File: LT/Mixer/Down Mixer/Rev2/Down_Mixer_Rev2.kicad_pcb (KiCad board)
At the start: 2 copper layers, 70.6 x 45.2 mm, 18 parts, among them J1 Conn_Coaxial, J2 Conn_Coaxial, J3 Conn_Coaxial, J4 Conn_01x02_Male, U1 SA602

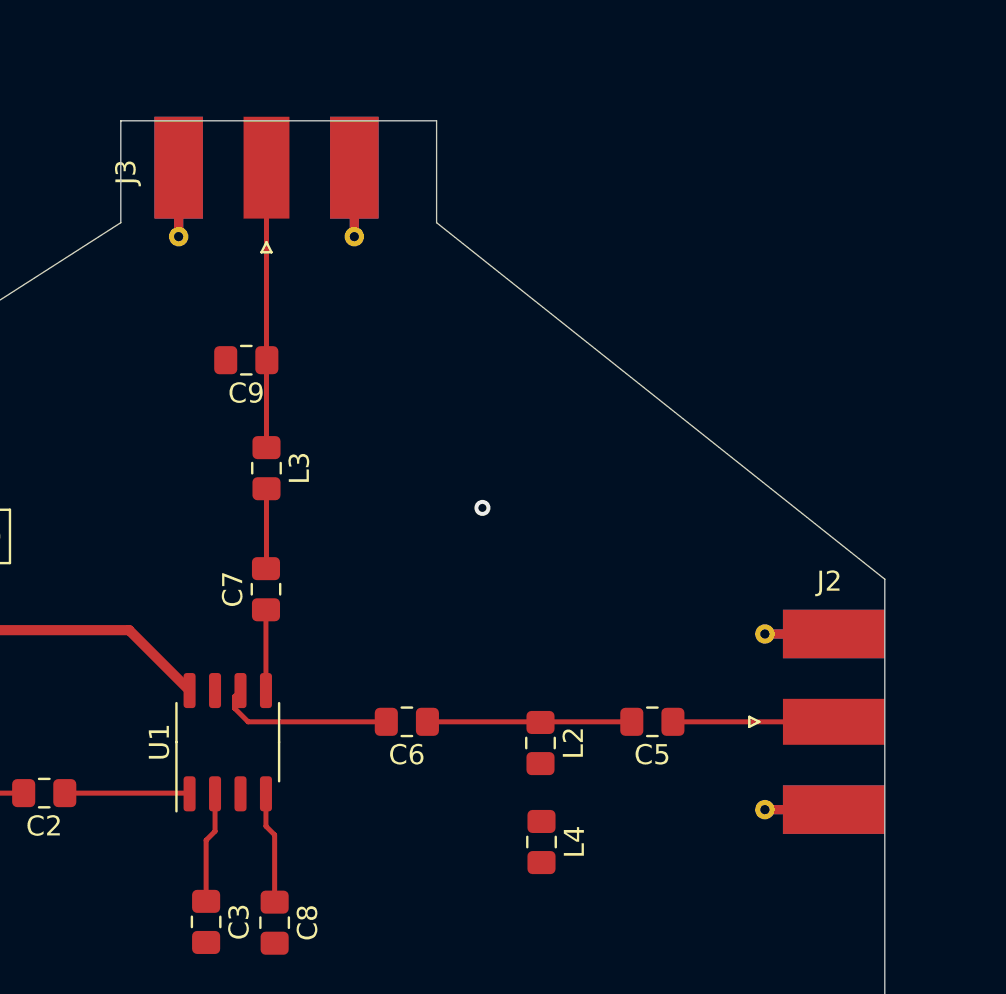
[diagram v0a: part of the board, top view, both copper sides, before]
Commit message: rotated inductor to reduce coupling
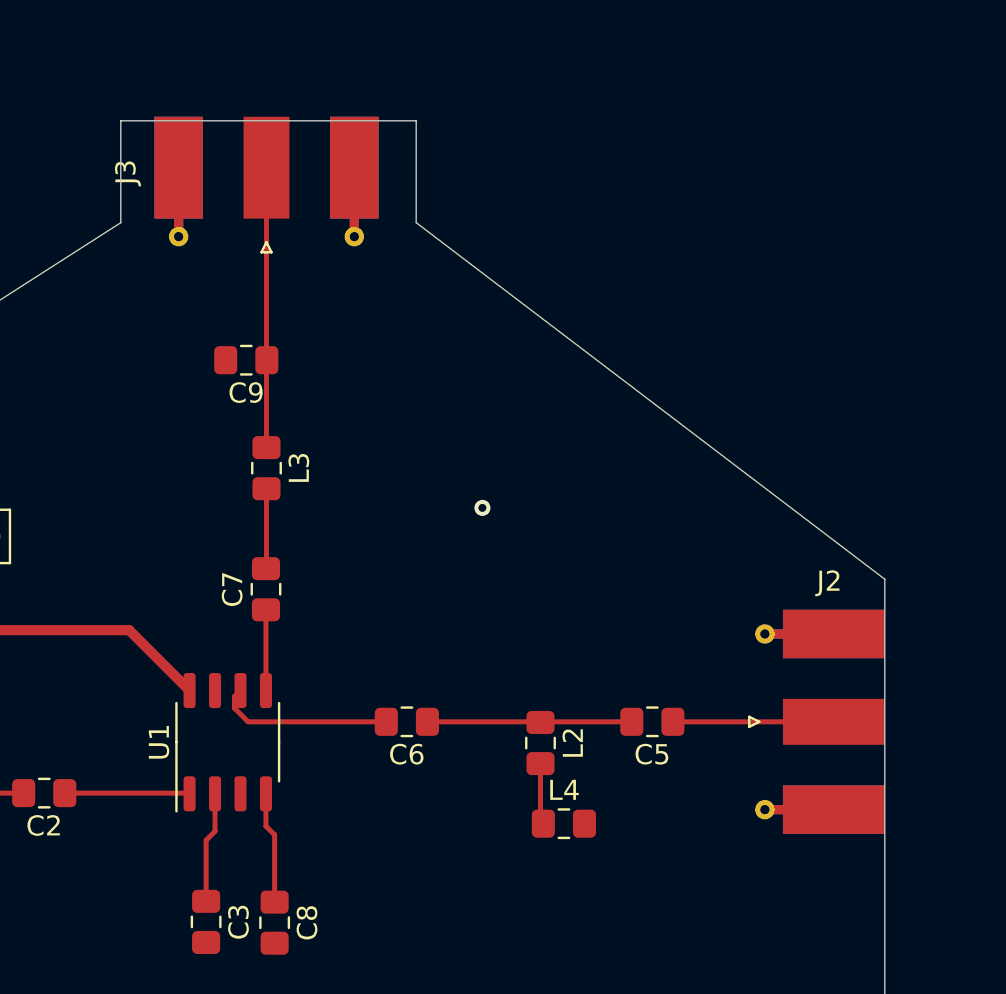
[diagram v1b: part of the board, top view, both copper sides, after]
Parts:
- moved L4 1.44 mm to (141.0, 86.4), turned to 0 degrees
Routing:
- net Net-(L2-Pad2): track 0.00 -> 2.91 mm
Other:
- outline, holes or cut-outs redrawn
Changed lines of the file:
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@@
     (thickness 1.6)
     (drawings 8)
-    (tracks 26)
+    (tracks 28)
     (zones 0)
     (modules 18)
@@
   )
   (module Inductor_SMD:L_0805_2012Metric_Pad1.15x1.40mm_HandSolder (layer F.Cu)
-    (at 139.8524 87.2744 270)
+    (at 140.97 86.36)
     (descr "Capacitor SMD 0805 (2012 Metric), square (rectangular) end terminal, IPC_7351 nominal with elongated pad for handsoldering. (Body size source: https://docs.google.com/spreadsheets/d/1BsfQQcO9C6DZCsRaXUlFlo91Tg2WpOkGARC1WS5S8t0/edit?usp=sharing), generated with kicad-footprint-generator")
     (tags "inductor handsolder")
     (attr smd)
-    (fp_text reference L4 (at 0 -1.65 90) (layer F.SilkS)
-      (effects (font (size 1 1) (thickness 0.15)))
-    )
-    (fp_text value 680n (at 0 1.65 90) (layer F.Fab)
-      (effects (font (size 1 1) (thickness 0.15)))
-    )
-    (fp_line (start -1 0.6) (end -1 -0.6) (layer F.Fab) (width 0.1))
-    (fp_line (start -1 -0.6) (end 1 -0.6) (layer F.Fab) (width 0.1))
-    (fp_line (start 1 -0.6) (end 1 0.6) (layer F.Fab) (width 0.1))
-    (fp_line (start 1 0.6) (end -1 0.6) (layer F.Fab) (width 0.1))
-    (fp_line (start -0.261252 -0.71) (end 0.261252 -0.71) (layer F.SilkS) (width 0.12))
-    (fp_line (start -0.261252 0.71) (end 0.261252 0.71) (layer F.SilkS) (width 0.12))
-    (fp_line (start -1.85 0.95) (end -1.85 -0.95) (layer F.CrtYd) (width 0.05))
-    (fp_line (start -1.85 -0.95) (end 1.85 -0.95) (layer F.CrtYd) (width 0.05))
-    (fp_line (start 1.85 -0.95) (end 1.85 0.95) (layer F.CrtYd) (width 0.05))
-    (fp_line (start 1.85 0.95) (end -1.85 0.95) (layer F.CrtYd) (width 0.05))
-    (fp_text user %R (at 0 0 90) (layer F.Fab)
-      (effects (font (size 0.5 0.5) (thickness 0.08)))
-    )
-    (pad 1 smd roundrect (at -1.025 0 270) (size 1.15 1.4) (layers F.Cu F.Paste F.Mask) (roundrect_rratio 0.217391)
+    (fp_text reference L4 (at 0 -1.65) (layer F.SilkS)
+      (effects (font (size 1 1) (thickness 0.15)))
+    )
+    (fp_text value 680n (at 0 1.65) (layer F.Fab)
+      (effects (font (size 1 1) (thickness 0.15)))
+    )
+    (fp_line (start -1 0.6) (end -1 -0.6) (layer F.Fab) (width 0.1))
+    (fp_line (start -1 -0.6) (end 1 -0.6) (layer F.Fab) (width 0.1))
+    (fp_line (start 1 -0.6) (end 1 0.6) (layer F.Fab) (width 0.1))
+    (fp_line (start 1 0.6) (end -1 0.6) (layer F.Fab) (width 0.1))
+    (fp_line (start -0.261252 -0.71) (end 0.261252 -0.71) (layer F.SilkS) (width 0.12))
+    (fp_line (start -0.261252 0.71) (end 0.261252 0.71) (layer F.SilkS) (width 0.12))
+    (fp_line (start -1.85 0.95) (end -1.85 -0.95) (layer F.CrtYd) (width 0.05))
+    (fp_line (start -1.85 -0.95) (end 1.85 -0.95) (layer F.CrtYd) (width 0.05))
+    (fp_line (start 1.85 -0.95) (end 1.85 0.95) (layer F.CrtYd) (width 0.05))
+    (fp_line (start 1.85 0.95) (end -1.85 0.95) (layer F.CrtYd) (width 0.05))
+    (fp_text user %R (at 0 0) (layer F.Fab)
+      (effects (font (size 0.5 0.5) (thickness 0.08)))
+    )
+    (pad 1 smd roundrect (at -1.025 0) (size 1.15 1.4) (layers F.Cu F.Paste F.Mask) (roundrect_rratio 0.217391)
       (net 14 "Net-(L2-Pad2)"))
-    (pad 2 smd roundrect (at 1.025 0 270) (size 1.15 1.4) (layers F.Cu F.Paste F.Mask) (roundrect_rratio 0.217391)
+    (pad 2 smd roundrect (at 1.025 0) (size 1.15 1.4) (layers F.Cu F.Paste F.Mask) (roundrect_rratio 0.217391)
       (net 2 GND))
     (model ${KISYS3DMOD}/Inductor_SMD.3dshapes/L_0805_2012Metric.wrl
@@
     )
   )
-  (gr_line (start 134.62 51.308) (end 134.62 56.388) (layer Edge.Cuts) (width 0.05))
-  (gr_line (start 118.872 51.308) (end 134.62 51.308) (layer Edge.Cuts) (width 0.05))
+  (gr_line (start 133.604 51.308) (end 133.604 56.388) (layer Edge.Cuts) (width 0.05))
+  (gr_line (start 118.872 51.308) (end 133.604 51.308) (layer Edge.Cuts) (width 0.05))
   (gr_line (start 118.872 56.388) (end 118.872 51.308) (layer Edge.Cuts) (width 0.05))
   (gr_line (start 156.972 74.168) (end 156.972 96.52) (layer Edge.Cuts) (width 0.05))
-  (gr_line (start 134.62 56.388) (end 156.972 74.168) (layer Edge.Cuts) (width 0.05))
+  (gr_line (start 133.604 56.388) (end 156.972 74.168) (layer Edge.Cuts) (width 0.05))
   (gr_line (start 86.36 77.216) (end 118.872 56.388) (layer Edge.Cuts) (width 0.05))
   (gr_line (start 86.36 96.52) (end 86.36 77.216) (layer Edge.Cuts) (width 0.05))
@@
   (segment (start 126.5428 86.9188) (end 126.111 86.487) (width 0.25) (layer F.Cu) (net 12))
   (segment (start 126.1364 53.6448) (end 126.1364 67.6058) (width 0.25) (layer F.Cu) (net 13))
+  (segment (start 139.8016 86.1986) (end 139.8524 86.2494) (width 0.25) (layer F.Cu) (net 14))
+  (segment (start 139.8016 83.3628) (end 139.8016 86.1986) (width 0.25) (layer F.Cu) (net 14))
   (zone (net 2) (net_name GND) (layer F.Cu) (hatch edge 0.508)
     (connect_pads yes (clearance 0.508))

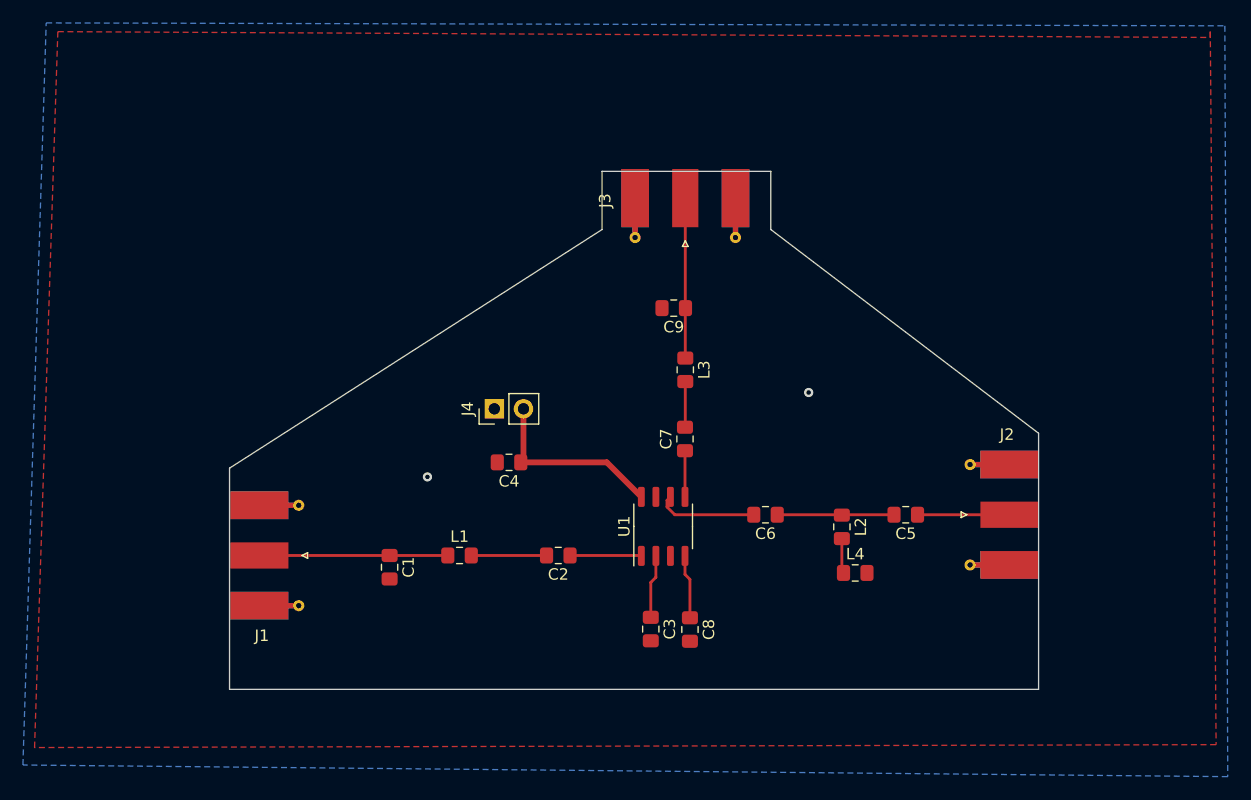
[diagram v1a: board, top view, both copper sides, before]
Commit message: swapped edge mount footprint. created gerber and drill files.
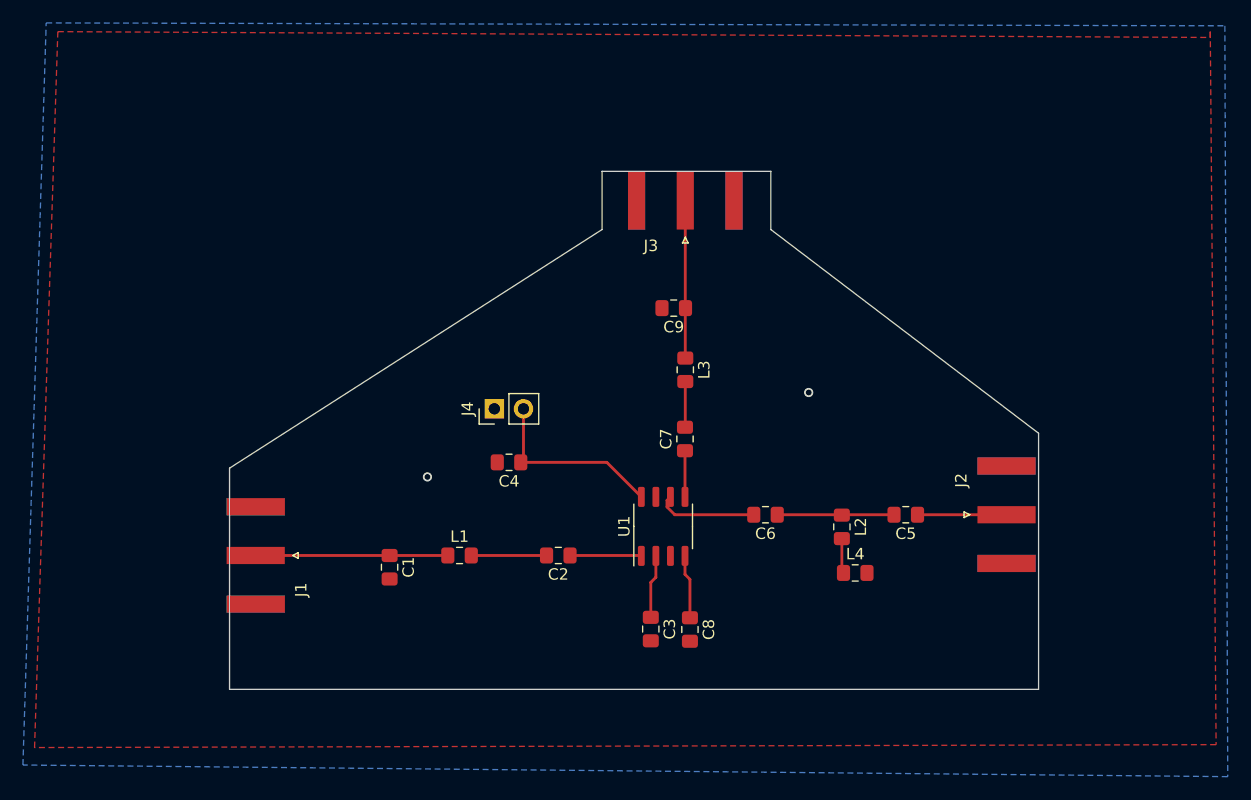
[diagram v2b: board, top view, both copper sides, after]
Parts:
- J1, J2, J3: footprint Connector_Coaxial:SMA_Molex_73251-1153_EdgeMount_Horizontal -> Connector_Coaxial:SMA_Amphenol_132289_EdgeMount
- moved J1 2.03 mm to (88.6, 84.8), turned to 180 degrees
- moved J3 1.52 mm to (126.1, 53.8), turned to 90 degrees
- moved J2 1.47 mm to (154.2, 81.3), turned to 0 degrees
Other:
- net class Default: clearance 0.2 -> 0.254; via_drill 0.4 -> 0.508
- rule trace_clearance: 0.2 -> 0.254
